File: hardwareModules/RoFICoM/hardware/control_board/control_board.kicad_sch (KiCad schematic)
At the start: 42 parts, among them J1 SkirtConnector, J2 M+, J26 BoardSkirtConnector, J27 SkirtConnector, J28 SkirtConnector, J3 M-, J4 SYS_CONN, J5 PWR_CONN_1, J6 PWR_CONN_2, U2 DRV8837C, U3 HX6306P332MR, U9 STM32G071CBUx

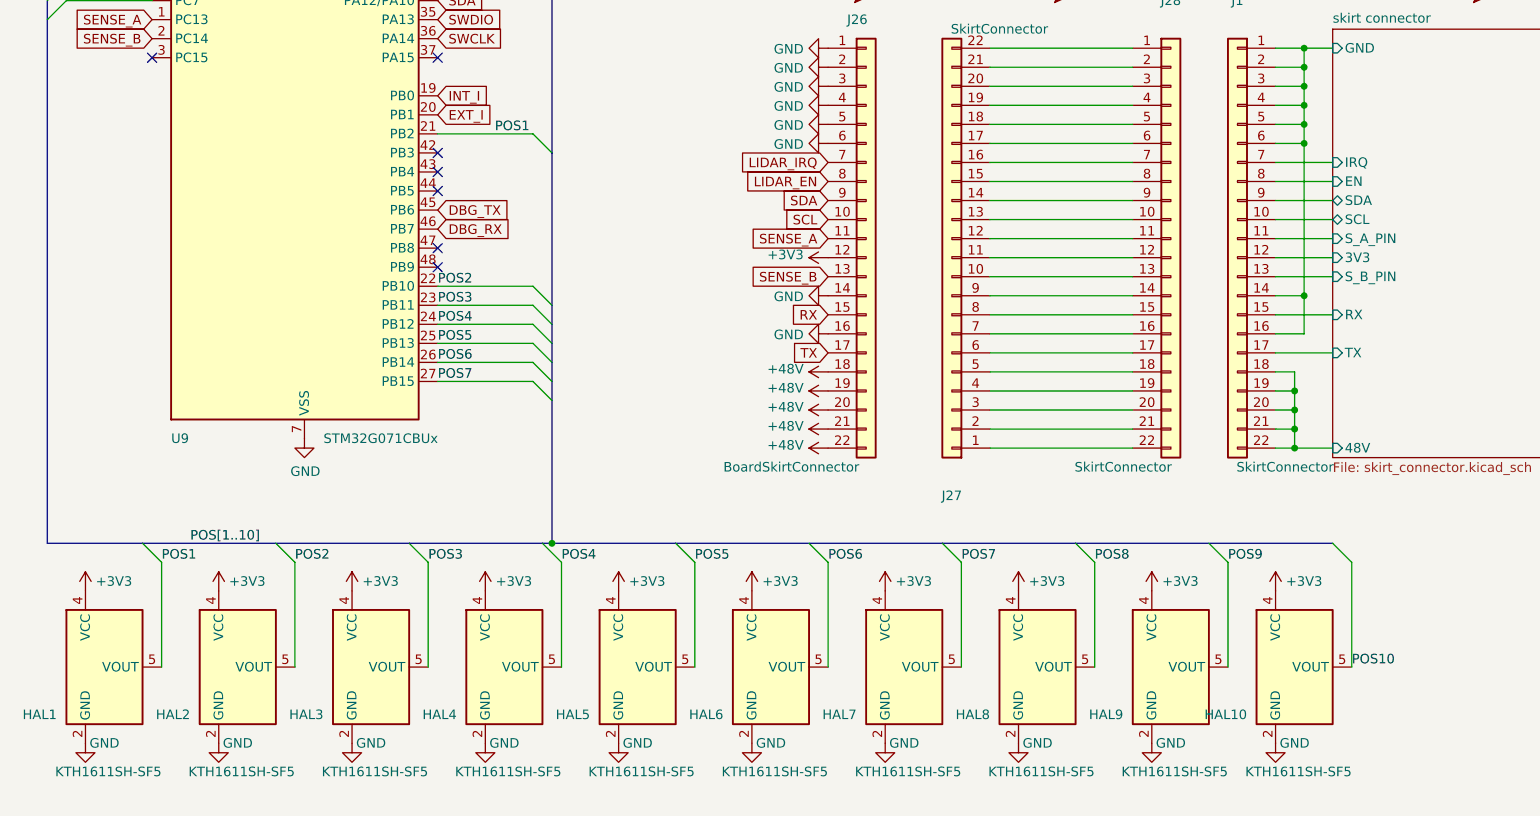
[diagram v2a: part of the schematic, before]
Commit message: roficom: Add Hall position sensor hardware
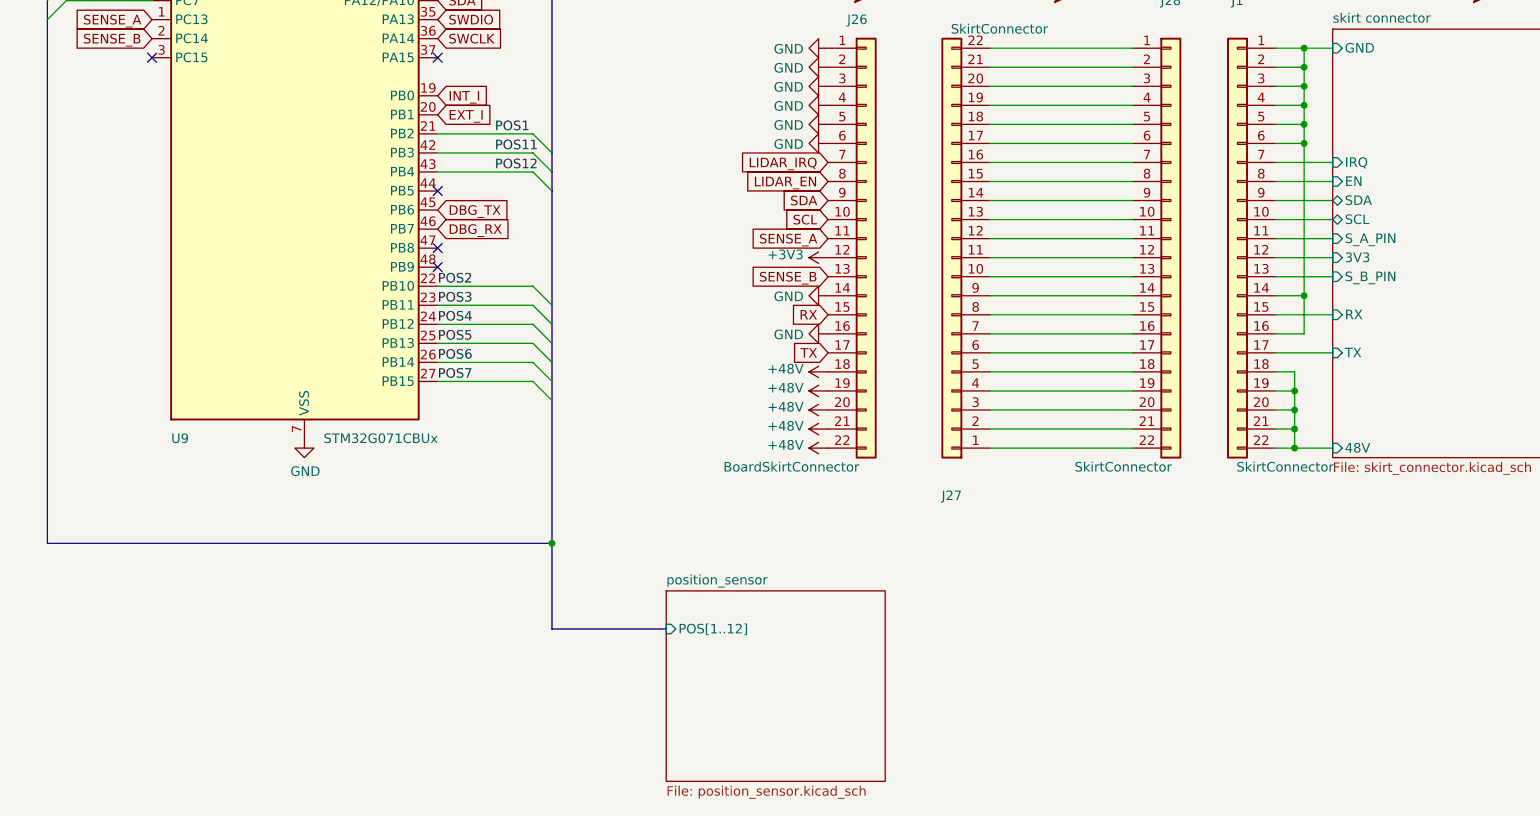
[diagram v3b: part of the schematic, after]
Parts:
- removed HAL1, HAL10, HAL2, HAL3, HAL4, HAL5, HAL6, HAL7, HAL8, HAL9: KTH1611SH-SF5, Package_TO_SOT_SMD:SOT-553, symbol rofi:KTH1611SH-SF5
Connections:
- net POS11: now reaches U9.42 (PB3)
- net POS12: now reaches U9.43 (PB4)
- no-connect marks 9 -> 7
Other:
- added sheet position_sensor (position_sensor.kicad_sch)
